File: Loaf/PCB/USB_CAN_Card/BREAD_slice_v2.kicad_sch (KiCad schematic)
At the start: 11 parts, among them J1 10018783-10200TLF, J2 USB_B, P1 USB_C_Plug_USB2.0, U1 MCP2210x-SO, U2 MCP2515-xSO

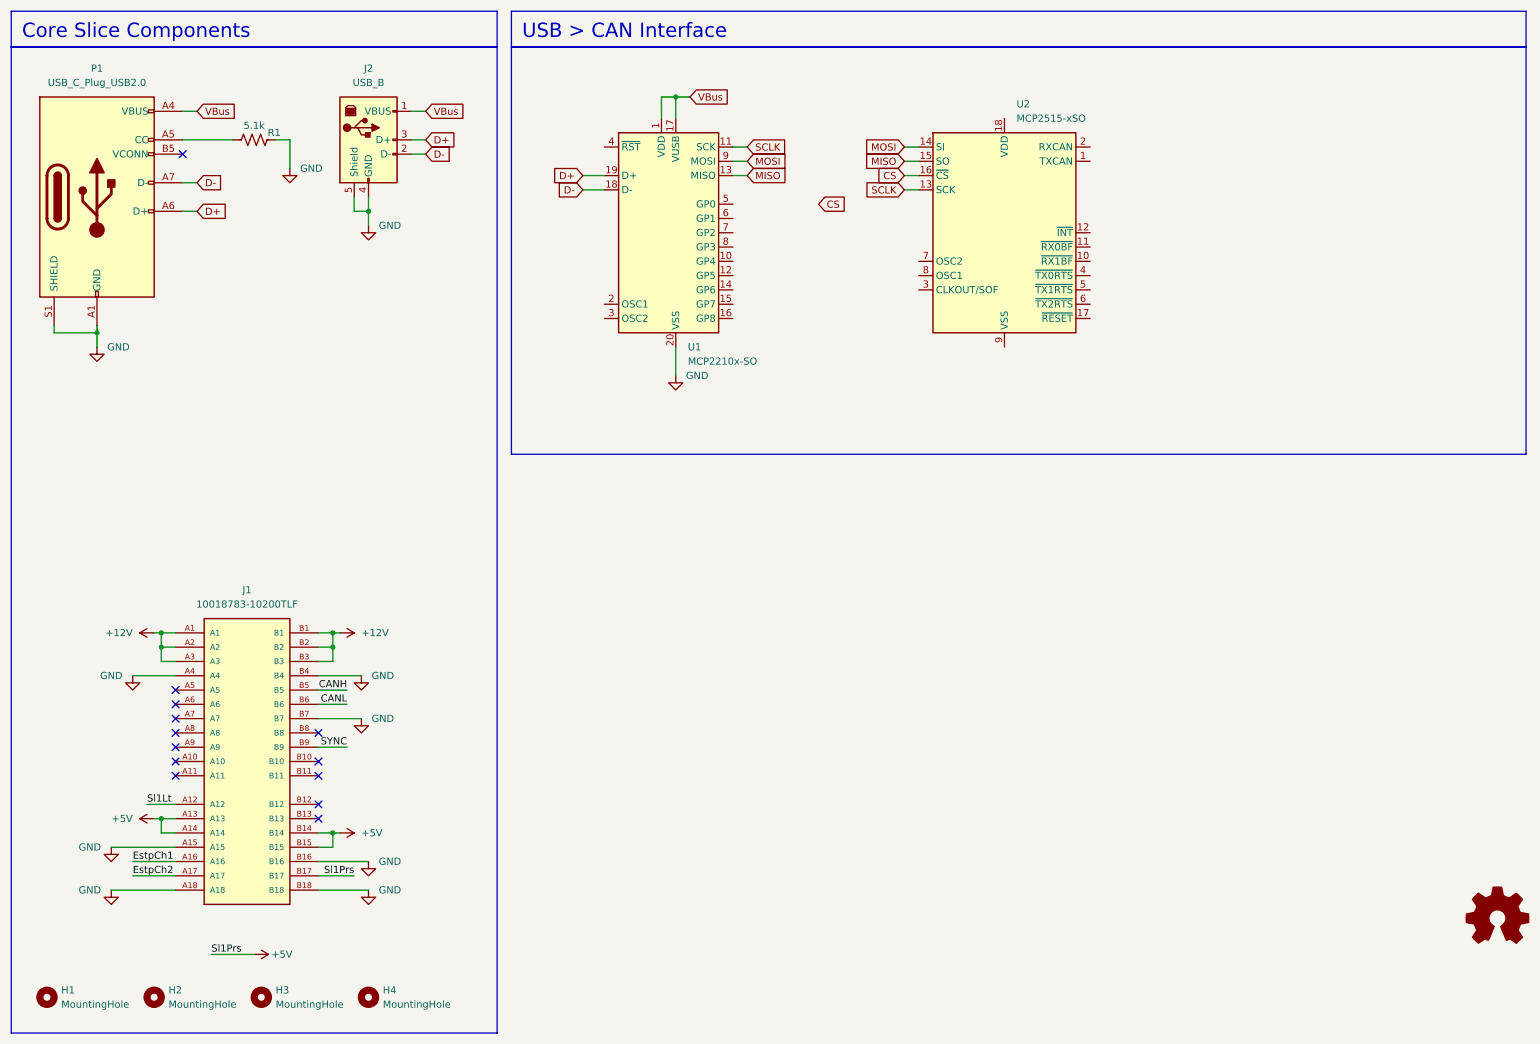
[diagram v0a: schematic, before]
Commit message: Added parts to USB-CAN Card
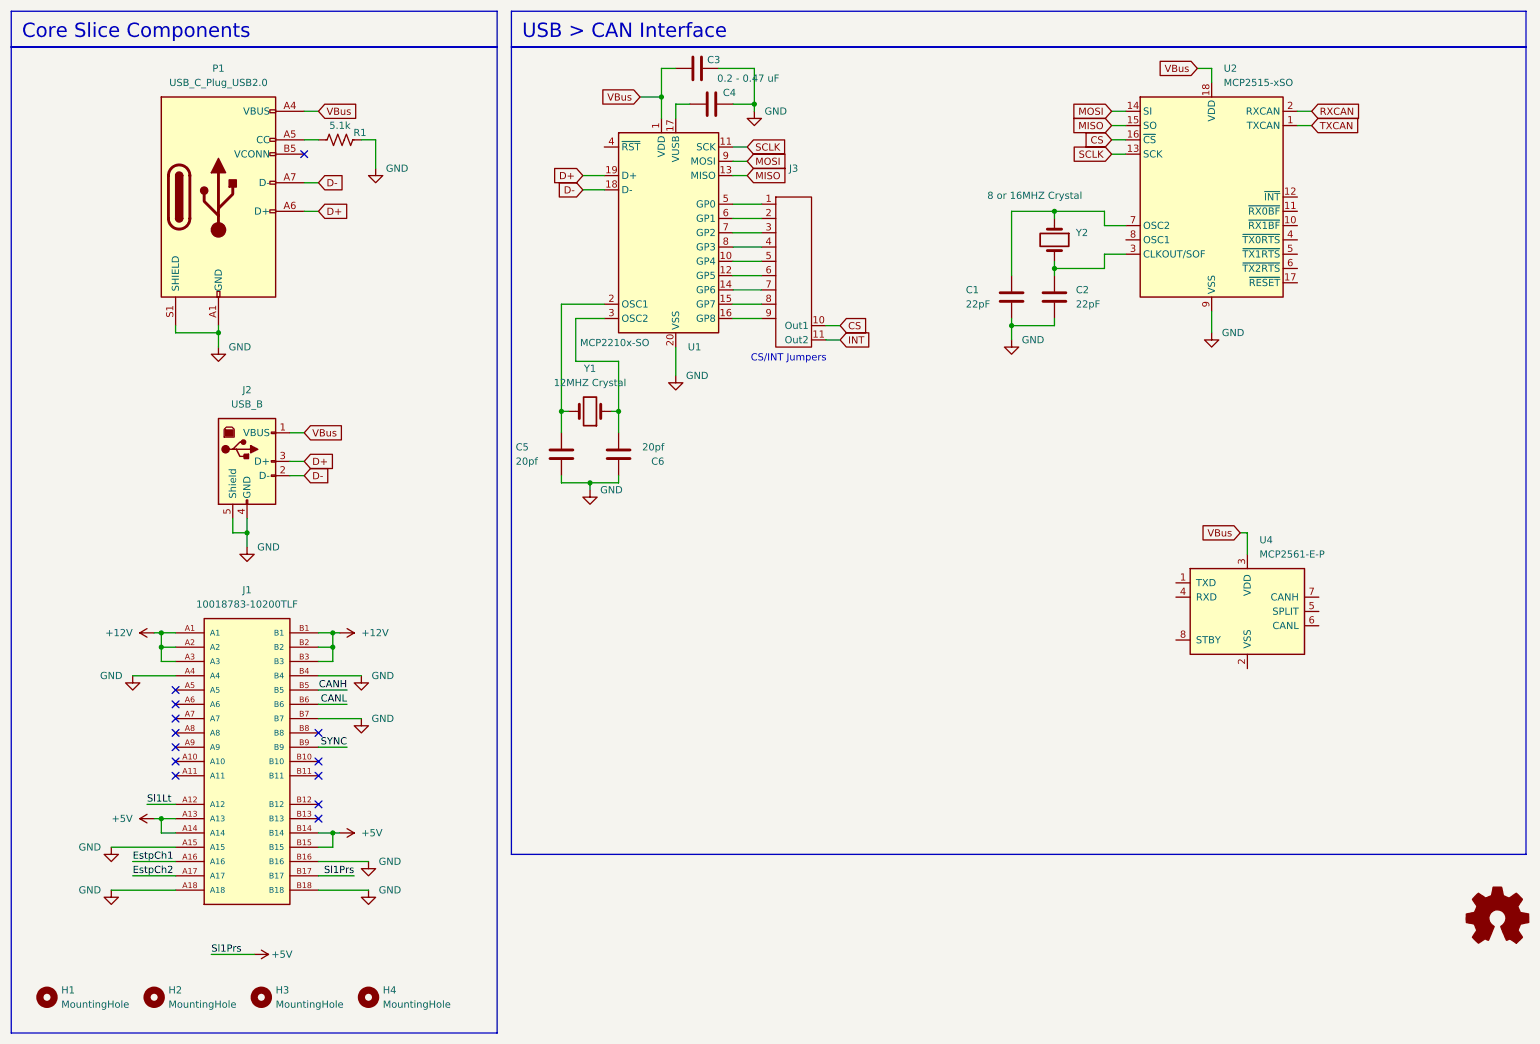
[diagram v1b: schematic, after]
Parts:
- added C1, C2, C4: 22pF, Capacitor_SMD:C_1206_3216Metric_Pad1.33x1.80mm_HandSolder, symbol Device:C
- added C3: 0.2 - 0.47 uF, Capacitor_SMD:C_1206_3216Metric_Pad1.33x1.80mm_HandSolder, symbol Device:C
- added C5, C6: 20pf, Capacitor_SMD:C_1206_3216Metric_Pad1.33x1.80mm_HandSolder, symbol Device:C
- added J3: ~, 3x9 Jumper, symbol Custom:3x9_Jumpers
- added U4: MCP2561-E-P, Package_DIP:DIP-8_W7.62mm, symbol Interface_CAN_LIN:MCP2561-E-P
- added Y1: 12MHZ Crystal, Crystal_HC49-4H_Vertical, symbol Device:Crystal
- added Y2: 8 or 16MHZ Crystal, Crystal_HC49-4H_Vertical, symbol Device:Crystal
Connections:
- net CS: now also J3.10 (Out1)
- net GND: now also U2.9 (VSS), C1.2, C2.2, C3.1, C4.1, C5.2, C6.1
- net VBus: now also U2.18 (VDD), C3.2, U4.3 (VDD); no longer U1.17 (VUSB)
- net at U1.10 (GP4): now also J3.5
- net at U1.12 (GP5): now also J3.6
- net at U1.14 (GP6): now also J3.7
- net at U1.15 (GP7): now also J3.8
- net at U1.16 (GP8): now also J3.9
- net at U1.2 (OSC1): now also C5.1, Y1.2
- net at U1.3 (OSC2): now also C6.2, Y1.1
- net at U1.5 (GP0): now also J3.1
- net at U1.6 (GP1): now also J3.2
- net at U1.7 (GP2): now also J3.3
- net at U1.8 (GP3): now also J3.4
- net TXCAN: now reaches U2.1 (TXCAN)
- net RXCAN: now reaches U2.2 (RXCAN)
- net at U2.3 (CLKOUT/SOF): now also C2.1, Y2.2
- net at U2.7 (OSC2): now also C1.1, Y2.1
- new net: C4.2, U1.17 (VUSB)
- new net INT: J3.11 (Out2)
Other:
- note added: "CS/INT Jumpers"
- moved on the sheet: J2, P1, R1, U2

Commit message: Updated IO slice schematic
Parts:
- J2: footprint (none) -> USB_B_OST_USB-B1HSxx_Horizontal
- J3: value ~ -> (none)
- P1: footprint (none) -> USB_C_Receptacle_GCT_USB4085

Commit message: USB Slice and slop test program
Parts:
- removed C1, C2: 22pF, Capacitor_SMD:C_1206_3216Metric_Pad1.33x1.80mm_HandSolder, symbol Device:C
- removed J3: (no value), 3x9 Jumper, symbol Custom:3x9_Jumpers
- removed P1: USB_C_Plug_USB2.0, USB_C_Receptacle_GCT_USB4085, symbol Connector:USB_C_Plug_USB2.0
- removed R1: 5.1k, R_1206_3216Metric, symbol Device:R_US
- removed U4: MCP2561-E-P, Package_DIP:DIP-8_W7.62mm, symbol Interface_CAN_LIN:MCP2561-E-P
- added C5, C6: 20pf, Capacitor_SMD:C_1206_3216Metric_Pad1.33x1.80mm_HandSolder, symbol Device:C
- added C7, C8: 0.47uF, C_1206_3216Metric_Pad1.33x1.80mm_HandSolder, symbol Device:C
- added R2, R3: 10k, Resistor_SMD:R_1206_3216Metric_Pad1.30x1.75mm_HandSolder, symbol Device:R_US
- added U3: MCP2561-E-P, Package_DIP:DIP-8_W7.62mm, symbol Interface_CAN_LIN:MCP2561-E-P
- U2: footprint Package_SO:SOIC-18W_7.5x11.6mm_P1.27mm -> DIP-18_W7.62mm
- Y2: value 8 or 16MHZ Crystal -> 16MHZ Crystal
- renumbered C3 to C1, C4 to C2, C5 to C3, C6 to C4, J2 to P2
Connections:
- net CANH: now also U3.7 (CANH)
- net CANL: now also U3.6 (CANL)
- net CS: now also U1.8 (GP3)
- net GND: now also C5.2, C6.2, C7.1, C8.1, R3.2, U3.2 (VSS)
- net INT: now also U1.10 (GP4), U2.12 (~{INT})
- net VBus: now also C7.2, C8.2, R2.2, U3.3 (VDD)
- net at U2.7 (OSC2): now also Y2.2, C5.1; no longer Y2.1
- net at U2.3 (CLKOUT/SOF): no longer Y2.2
- net at U2.17 (~{RESET}): now also R2.1
- net at U2.8 (OSC1): now also Y2.1, C6.1
- net RXCAN renamed CANRX
- net CANRX: now also U3.4 (RXD)
- net TXCAN renamed CANTX
- net CANTX: now also U3.1 (TXD)
- new net: R3.1, U3.8 (STBY)
- no-connect marks 13 -> 18
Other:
- note added: "CAN Transciever"
- note added: "CAN controller"
- note removed: "CS/INT Jumpers"

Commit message: Updated PCB Schematics
Added correct capacitor values and one missing resistor on USB card
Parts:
- added R4: 10k, Resistor_SMD:R_1206_3216Metric_Pad1.30x1.75mm_HandSolder, symbol Device:R_US
- C1: value 0.2 - 0.47 uF -> 2uF
- C2: value 22pF -> 0.22-0.47uF
- C7, C8: value 0.47uF -> 0.1uF
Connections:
- net VBus: now also R4.2
- net at U1.4 (~{RST}): now also R4.1
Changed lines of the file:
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@@
 	(wire
 		(pts
+			(xy 118.11 38.1) (xy 119.38 38.1)
+		)
+		(stroke
+			(width 0)
+			(type default)
+		)
+	)
+	(wire
+		(pts
 			(xy 182.88 130.81) (xy 184.15 130.81)
 		)
@@
 		)
 	)
+	(global_label "VBus"
+		(shape input)
+		(at 110.49 38.1 180)
+		(fields_autoplaced yes)
+		(effects
+			(font
+				(size 1.27 1.27)
+			)
+			(justify right)
+		)
+		(property "Intersheetrefs" "${INTERSHEET_REFS}"
+			(at 102.9691 38.1 0)
+			(hide yes)
+			(show_name no)
+			(do_not_autoplace no)
+			(effects
+				(font
+					(size 1.27 1.27)
+				)
+				(justify right)
+			)
+		)
+	)
 	(global_label "CS"
 		(shape input)
@@
 			)
 		)
-		(property "Value" "0.47uF"
+		(property "Value" "0.1uF"
 			(at 193.04 125.984 90)
 			(show_name no)
@@
 		(dnp no)
 		(property "Reference" "C2"
-			(at 140.462 28.448 90)
+			(at 140.208 28.956 90)
 			(show_name no)
 			(do_not_autoplace no)
@@
 			)
 		)
-		(property "Value" "22pF"
-			(at 137.16 22.352 0)
-			(hide yes)
+		(property "Value" "0.22-0.47uF"
+			(at 132.334 34.036 90)
 			(show_name no)
 			(do_not_autoplace no)
@@
 			)
 		)
-		(property "Value" "0.47uF"
+		(property "Value" "0.1uF"
 			(at 111.76 115.316 90)
 			(show_name no)
@@
 	)
 	(symbol
+		(lib_id "Device:R_US")
+		(at 114.3 38.1 270)
+		(unit 1)
+		(body_style 1)
+		(exclude_from_sim no)
+		(in_bom yes)
+		(on_board yes)
+		(in_pos_files yes)
+		(dnp no)
+		(property "Reference" "R4"
+			(at 114.3 35.56 90)
+			(show_name no)
+			(do_not_autoplace no)
+			(effects
+				(font
+					(size 1.27 1.27)
+				)
+			)
+		)
+		(property "Value" "10k"
+			(at 114.3 41.148 90)
+			(show_name no)
+			(do_not_autoplace no)
+			(effects
+				(font
+					(size 1.27 1.27)
+				)
+			)
+		)
+		(property "Footprint" "Resistor_SMD:R_1206_3216Metric_Pad1.30x1.75mm_HandSolder"
+			(at 114.046 39.116 90)
+			(hide yes)
+			(show_name no)
+			(do_not_autoplace no)
+			(effects
+				(font
+					(size 1.27 1.27)
+				)
+			)
+		)
+		(property "Datasheet" ""
+			(at 114.3 38.1 0)
+			(hide yes)
+			(show_name no)
+			(do_not_autoplace no)
+			(effects
+				(font
+					(size 1.27 1.27)
+				)
+			)
+		)
+		(property "Description" ""
+			(at 114.3 38.1 0)
+			(hide yes)
+			(show_name no)
+			(do_not_autoplace no)
+			(effects
+				(font
+					(size 1.27 1.27)
+				)
+			)
+		)
+		(pin "1"
+		)
+		(pin "2"
+		)
+		(instances
+			(project "BREAD_slice_v2"
+				(path "/7f913798-a7fb-4519-b930-d05e163d3032"
+					(reference "R4")
+					(unit 1)
+				)
+			)
+		)
+	)
+	(symbol
 		(lib_id "Device:C")
 		(at 111.76 92.71 0)
@@
 			)
 		)
-		(property "Value" "0.2 - 0.47 uF"
+		(property "Value" "2uF"
 			(at 139.446 25.908 90)
 			(show_name no)

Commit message: Slight updates
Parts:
- C1: value 2uF -> 1uF
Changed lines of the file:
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@@
 	(text "CAN controller"
 		(exclude_from_sim no)
-		(at 130.302 106.68 0)
+		(at 129.286 110.744 0)
 		(effects
 			(font
@@
 			)
 		)
-		(property "Value" "2uF"
+		(property "Value" "1uF"
 			(at 139.446 25.908 90)
 			(show_name no)

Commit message: Peter recommended PCB changes
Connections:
- net +12V: no longer J1.A1, J1.A2, J1.A3
- new net: J1.A1, J1.A2, J1.A3
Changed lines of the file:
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@@
-	)
-	(symbol
-		(lib_id "power:+12V")
-		(at 39.37 124.46 90)
-		(unit 1)
-		(body_style 1)
-		(exclude_from_sim no)
-		(in_bom yes)
-		(on_board yes)
-		(in_pos_files yes)
-		(dnp no)
-		(fields_autoplaced yes)
-		(property "Reference" "#PWR07"
-			(at 43.18 124.46 0)
-			(hide yes)
-			(show_name no)
-			(do_not_autoplace no)
-			(effects
-				(font
-					(size 1.27 1.27)
-				)
-			)
-		)
-		(property "Value" "+12V"
-			(at 35.56 124.4599 90)
-			(show_name no)
-			(do_not_autoplace no)
-			(effects
-				(font
-					(size 1.27 1.27)
-				)
-				(justify left)
-			)
-		)
-		(property "Footprint" ""
-			(at 39.37 124.46 0)
-			(hide yes)
-			(show_name no)
-			(do_not_autoplace no)
-			(effects
-				(font
-					(size 1.27 1.27)
-				)
-			)
-		)
-		(property "Datasheet" ""
-			(at 39.37 124.46 0)
-			(hide yes)
-			(show_name no)
-			(do_not_autoplace no)
-			(effects
-				(font
-					(size 1.27 1.27)
-				)
-			)
-		)
-		(property "Description" "Power symbol creates a global label with name \"+12V\""
-			(at 39.37 124.46 0)
-			(hide yes)
-			(show_name no)
-			(do_not_autoplace no)
-			(effects
-				(font
-					(size 1.27 1.27)
-				)
-			)
-		)
-		(pin "1"
-		)
-		(instances
-			(project "BREAD_slice_v2"
-				(path "/7f913798-a7fb-4519-b930-d05e163d3032"
-					(reference "#PWR07")
-					(unit 1)
-				)
-			)
-		)
 	)
 	(symbol
@@
 		(property "Value" "+12V"
 			(at 76.2 124.4601 90)
-			(show_name no)
-			(do_not_autoplace no)
+			(hide yes)
+			(show_name no)
+			(do_not_autoplace no)
